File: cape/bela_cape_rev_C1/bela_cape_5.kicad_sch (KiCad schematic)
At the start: 27 parts, among them IC2 TLV320AIC3104, IC3 MIC5317

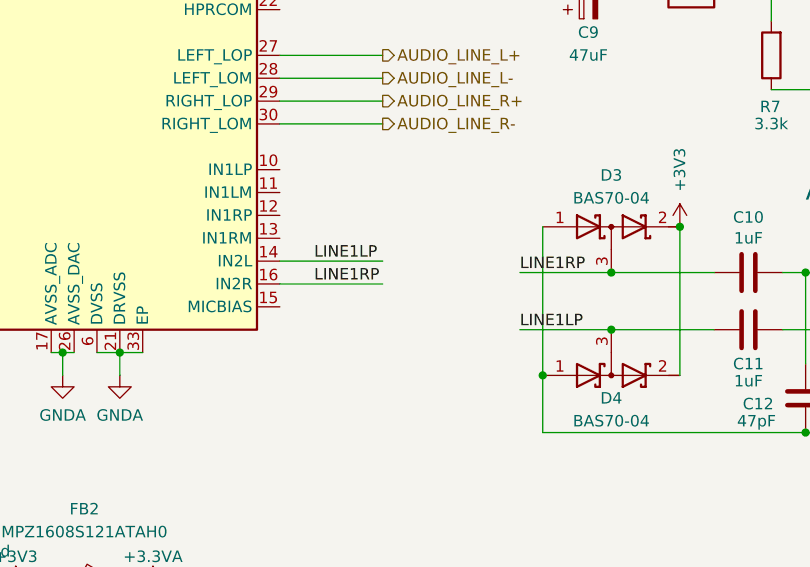
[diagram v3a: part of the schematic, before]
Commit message: First complete iteration of C1 cape layout
(cherry picked from commit 0ee733c70b42f416809330055e007cefcdb105fa)
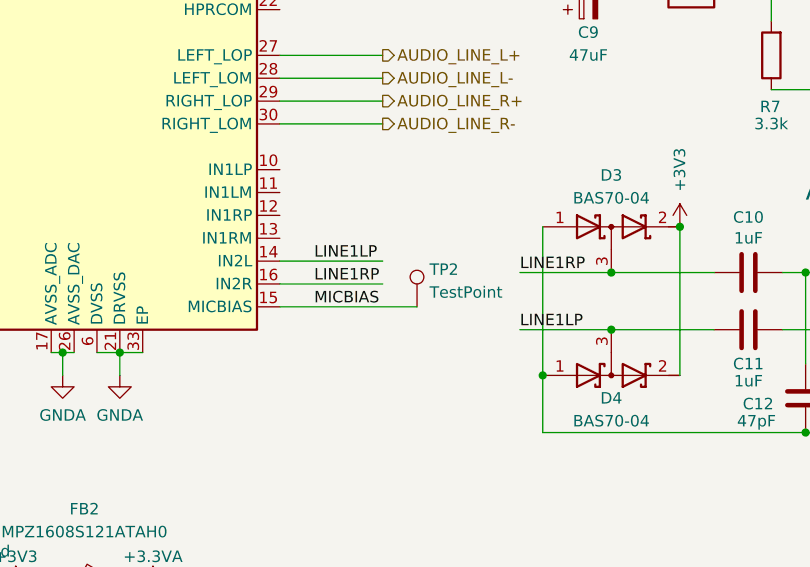
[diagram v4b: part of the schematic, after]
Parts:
- added TP2: TestPoint, TestPoint:TestPoint_THTPad_D2.0mm_Drill1.0mm, symbol Connector:TestPoint
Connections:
- net MICBIAS: now reaches IC2.15 (MICBIAS)
- net MICBIAS: now also TP2.1
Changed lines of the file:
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@@
+    (stroke (width 0) (type default) (color 0 0 0 0))
+  )
+  (wire (pts (xy 72.39 82.55) (xy 87.63 82.55))
     (stroke (width 0) (type default) (color 0 0 0 0))
   )
@@
   )
   (label "AUD_HPLOUT" (at 73.66 41.91 0)
+    (effects (font (size 1.27 1.27)) (justify left bottom))
+  )
+  (label "MICBIAS" (at 76.2 82.55 0)
     (effects (font (size 1.27 1.27)) (justify left bottom))
   )
@@
     (pin "2")
   )
+  (symbol (lib_id "Connector:TestPoint") (at 87.63 82.55 0) (unit 1)
+    (in_bom yes) (on_board yes) (fields_autoplaced)
+    (property "Reference" "TP2" (id 0) (at 89.027 78.4133 0)
+      (effects (font (size 1.27 1.27)) (justify left))
+    )
+    (property "Value" "TestPoint" (id 1) (at 89.027 80.9502 0)
+      (effects (font (size 1.27 1.27)) (justify left))
+    )
+    (property "Footprint" "TestPoint:TestPoint_THTPad_D2.0mm_Drill1.0mm" (id 2) (at 92.71 82.55 0)
+      (effects (font (size 1.27 1.27)) hide)
+    )
+    (property "Datasheet" "~" (id 3) (at 92.71 82.55 0)
+      (effects (font (size 1.27 1.27)) hide)
+    )
+    (pin "1")
+  )
   (symbol (lib_id "Device:C") (at 38.1 132.08 0) (unit 1)
